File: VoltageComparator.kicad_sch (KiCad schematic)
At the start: 7 parts, among them U4 74LS08, U5 LM358

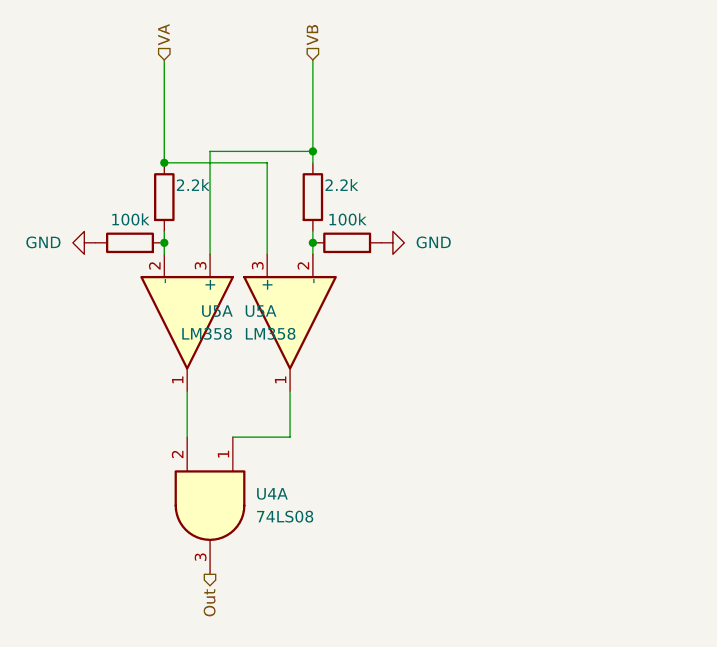
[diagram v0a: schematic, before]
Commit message: Added FSM, Button, 555 timer, changed shift registers
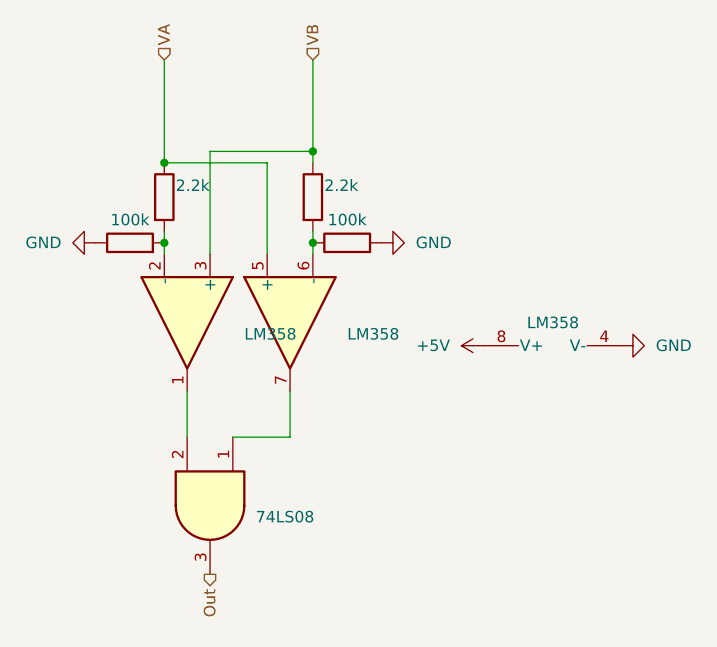
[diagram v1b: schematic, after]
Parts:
- added unit 2 of U18
- renumbered R9 to R5, R10 to R6, R11 to R7, R12 to R8, U5 to U18, U4 to U5
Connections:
- net GND: now also U18.4 (V-)
- net VA: now also U18.5 (+); no longer U18.3 (+)
- net at U5.1: now also U18.7; no longer U18.1
- net at R7.2, R8.1: now also U18.6 (-); no longer U18.2 (-)
- new net +5V: U18.8 (V+)
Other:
- title: (none) -> Voltage Tolerance Comparator

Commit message: Started PCB Work
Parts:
- removed unit 3 of U18
- R10: renamed from R7; value 2.2k -> 10k; footprint (none) -> Resistor_SMD:R_0805_2012Metric_Pad1.20x1.40mm_HandSolder
- R11: renamed from R8; value 100k -> 200k; footprint (none) -> Resistor_SMD:R_0805_2012Metric_Pad1.20x1.40mm_HandSolder
- R8: renamed from R5; value 100k -> 200k; footprint (none) -> Resistor_SMD:R_0805_2012Metric_Pad1.20x1.40mm_HandSolder
- R9: renamed from R6; footprint (none) -> Resistor_SMD:R_0805_2012Metric_Pad1.20x1.40mm_HandSolder
- U18: value LM358 -> LM324; footprint (none) -> Package_SO:SOIC-14_3.9x8.7mm_P1.27mm; symbol Amplifier_Operational:LM358 -> Amplifier_Operational:LM324
- U19: renamed from U5; footprint (none) -> Package_SO:SOIC-14_3.9x8.7mm_P1.27mm

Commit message: routed
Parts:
- renumbered R9 to R10, R10 to R11, R11 to R12, R8 to R9
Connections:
- net VA: now also U18.10 (+); no longer U18.5 (+)
- net VB: now also U18.12 (+); no longer U18.3 (+)
- net at U19.1: now also U18.8; no longer U18.7
- net at U19.2: now also U18.14; no longer U18.1
- net at R10.2, R9.2: now also U18.13 (-); no longer U18.2 (-)
- net at R11.2, R12.1: now also U18.9 (-); no longer U18.6 (-)
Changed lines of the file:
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@@
 		(on_board yes)
 		(dnp no)
-		(fields_autoplaced yes)
 		(property "Reference" "U19"
 			(at 58.42 95.2416 90)
@@
 		(dnp no)
 		(fields_autoplaced yes)
-		(property "Reference" "#PWR087"
+		(property "Reference" "#PWR088"
 			(at 78.74 67.31 0)
 			(effects
@@
 			(project "ECE145Mastermind"
 				(path "/8c64fe8a-5d6b-41bc-b3a3-9bda7b2e0f2c/218d925b-79f6-474b-97b2-c0ad78559cda"
-					(reference "#PWR091")
-					(unit 1)
-				)
-				(path "/8c64fe8a-5d6b-41bc-b3a3-9bda7b2e0f2c/4f59e726-7fd4-4ef0-8dbb-7a41976aa953"
-					(reference "#PWR087")
-					(unit 1)
-				)
-				(path "/8c64fe8a-5d6b-41bc-b3a3-9bda7b2e0f2c/acb554fe-df67-46ea-bc1c-079edbbfc216"
-					(reference "#PWR089")
-					(unit 1)
-				)
-				(path "/8c64fe8a-5d6b-41bc-b3a3-9bda7b2e0f2c/d4674d5d-47f2-4c8d-9fae-4e866cda3652"
-					(reference "#PWR093")
+					(reference "#PWR092")
+					(unit 1)
+				)
+				(path "/8c64fe8a-5d6b-41bc-b3a3-9bda7b2e0f2c/4f59e726-7fd4-4ef0-8dbb-7a41976aa953"
+					(reference "#PWR088")
+					(unit 1)
+				)
+				(path "/8c64fe8a-5d6b-41bc-b3a3-9bda7b2e0f2c/acb554fe-df67-46ea-bc1c-079edbbfc216"
+					(reference "#PWR090")
+					(unit 1)
+				)
+				(path "/8c64fe8a-5d6b-41bc-b3a3-9bda7b2e0f2c/d4674d5d-47f2-4c8d-9fae-4e866cda3652"
+					(reference "#PWR094")
 					(unit 1)
 				)
@@
 		(on_board yes)
 		(dnp no)
-		(property "Reference" "R9"
+		(property "Reference" "R10"
 			(at 50.8 60.9599 0)
 			(effects
@@
 			(project "ECE145Mastermind"
 				(path "/8c64fe8a-5d6b-41bc-b3a3-9bda7b2e0f2c/218d925b-79f6-474b-97b2-c0ad78559cda"
-					(reference "R17")
-					(unit 1)
-				)
-				(path "/8c64fe8a-5d6b-41bc-b3a3-9bda7b2e0f2c/4f59e726-7fd4-4ef0-8dbb-7a41976aa953"
-					(reference "R9")
-					(unit 1)
-				)
-				(path "/8c64fe8a-5d6b-41bc-b3a3-9bda7b2e0f2c/acb554fe-df67-46ea-bc1c-079edbbfc216"
-					(reference "R13")
-					(unit 1)
-				)
-				(path "/8c64fe8a-5d6b-41bc-b3a3-9bda7b2e0f2c/d4674d5d-47f2-4c8d-9fae-4e866cda3652"
-					(reference "R21")
+					(reference "R18")
+					(unit 1)
+				)
+				(path "/8c64fe8a-5d6b-41bc-b3a3-9bda7b2e0f2c/4f59e726-7fd4-4ef0-8dbb-7a41976aa953"
+					(reference "R10")
+					(unit 1)
+				)
+				(path "/8c64fe8a-5d6b-41bc-b3a3-9bda7b2e0f2c/acb554fe-df67-46ea-bc1c-079edbbfc216"
+					(reference "R14")
+					(unit 1)
+				)
+				(path "/8c64fe8a-5d6b-41bc-b3a3-9bda7b2e0f2c/d4674d5d-47f2-4c8d-9fae-4e866cda3652"
+					(reference "R22")
 					(unit 1)
 				)
@@
 		(dnp no)
 		(fields_autoplaced yes)
-		(property "Reference" "#PWR086"
+		(property "Reference" "#PWR087"
 			(at 34.29 67.31 0)
 			(effects
@@
 			(project "ECE145Mastermind"
 				(path "/8c64fe8a-5d6b-41bc-b3a3-9bda7b2e0f2c/218d925b-79f6-474b-97b2-c0ad78559cda"
-					(reference "#PWR090")
-					(unit 1)
-				)
-				(path "/8c64fe8a-5d6b-41bc-b3a3-9bda7b2e0f2c/4f59e726-7fd4-4ef0-8dbb-7a41976aa953"
-					(reference "#PWR086")
-					(unit 1)
-				)
-				(path "/8c64fe8a-5d6b-41bc-b3a3-9bda7b2e0f2c/acb554fe-df67-46ea-bc1c-079edbbfc216"
-					(reference "#PWR088")
-					(unit 1)
-				)
-				(path "/8c64fe8a-5d6b-41bc-b3a3-9bda7b2e0f2c/d4674d5d-47f2-4c8d-9fae-4e866cda3652"
-					(reference "#PWR092")
+					(reference "#PWR091")
+					(unit 1)
+				)
+				(path "/8c64fe8a-5d6b-41bc-b3a3-9bda7b2e0f2c/4f59e726-7fd4-4ef0-8dbb-7a41976aa953"
+					(reference "#PWR087")
+					(unit 1)
+				)
+				(path "/8c64fe8a-5d6b-41bc-b3a3-9bda7b2e0f2c/acb554fe-df67-46ea-bc1c-079edbbfc216"
+					(reference "#PWR089")
+					(unit 1)
+				)
+				(path "/8c64fe8a-5d6b-41bc-b3a3-9bda7b2e0f2c/d4674d5d-47f2-4c8d-9fae-4e866cda3652"
+					(reference "#PWR093")
 					(unit 1)
 				)
@@
 		(on_board yes)
 		(dnp no)
-		(property "Reference" "R10"
+		(property "Reference" "R11"
 			(at 67.31 60.9599 0)
 			(effects
@@
 			(project "ECE145Mastermind"
 				(path "/8c64fe8a-5d6b-41bc-b3a3-9bda7b2e0f2c/218d925b-79f6-474b-97b2-c0ad78559cda"
-					(reference "R18")
-					(unit 1)
-				)
-				(path "/8c64fe8a-5d6b-41bc-b3a3-9bda7b2e0f2c/4f59e726-7fd4-4ef0-8dbb-7a41976aa953"
-					(reference "R10")
-					(unit 1)
-				)
-				(path "/8c64fe8a-5d6b-41bc-b3a3-9bda7b2e0f2c/acb554fe-df67-46ea-bc1c-079edbbfc216"
-					(reference "R14")
-					(unit 1)
-				)
-				(path "/8c64fe8a-5d6b-41bc-b3a3-9bda7b2e0f2c/d4674d5d-47f2-4c8d-9fae-4e866cda3652"
-					(reference "R22")
+					(reference "R19")
+					(unit 1)
+				)
+				(path "/8c64fe8a-5d6b-41bc-b3a3-9bda7b2e0f2c/4f59e726-7fd4-4ef0-8dbb-7a41976aa953"
+					(reference "R11")
+					(unit 1)
+				)
+				(path "/8c64fe8a-5d6b-41bc-b3a3-9bda7b2e0f2c/acb554fe-df67-46ea-bc1c-079edbbfc216"
+					(reference "R15")
+					(unit 1)
+				)
+				(path "/8c64fe8a-5d6b-41bc-b3a3-9bda7b2e0f2c/d4674d5d-47f2-4c8d-9fae-4e866cda3652"
+					(reference "R23")
 					(unit 1)
 				)
@@
 		(at 62.23 76.2 90)
 		(mirror x)
-		(unit 2)
+		(unit 3)
 		(exclude_from_sim no)
 		(in_bom yes)
@@
 		)
 		(property "Value" "LM324"
-			(at 68.58 76.1999 90)
+			(at 68.58 77.4699 90)
 			(effects
 				(font
@@
 				(path "/8c64fe8a-5d6b-41bc-b3a3-9bda7b2e0f2c/4f59e726-7fd4-4ef0-8dbb-7a41976aa953"
 					(reference "U18")
+					(unit 3)
+				)
+				(path "/8c64fe8a-5d6b-41bc-b3a3-9bda7b2e0f2c/acb554fe-df67-46ea-bc1c-079edbbfc216"
+					(reference "U18")
 					(unit 2)
-				)
-				(path "/8c64fe8a-5d6b-41bc-b3a3-9bda7b2e0f2c/acb554fe-df67-46ea-bc1c-079edbbfc216"
-					(reference "U18")
-					(unit 4)
 				)
 				(path "/8c64fe8a-5d6b-41bc-b3a3-9bda7b2e0f2c/d4674d5d-47f2-4c8d-9fae-4e866cda3652"
@@
 		(lib_id "Amplifier_Operational:LM324")
 		(at 50.8 76.2 270)
-		(unit 1)
+		(unit 4)
 		(exclude_from_sim no)
 		(in_bom yes)
@@
 		)
 		(property "Value" "LM324"
-			(at 57.15 76.1999 90)
+			(at 57.15 77.4699 90)
 			(effects
 				(font
@@
 				(path "/8c64fe8a-5d6b-41bc-b3a3-9bda7b2e0f2c/4f59e726-7fd4-4ef0-8dbb-7a41976aa953"
 					(reference "U18")
-					(unit 1)
+					(unit 4)
 				)
 				(path "/8c64fe8a-5d6b-41bc-b3a3-9bda7b2e0f2c/acb554fe-df67-46ea-bc1c-079edbbfc216"
 					(reference "U18")
-					(unit 3)
+					(unit 1)
 				)
 				(path "/8c64fe8a-5d6b-41bc-b3a3-9bda7b2e0f2c/d4674d5d-47f2-4c8d-9fae-4e866cda3652"
@@
 		(on_board yes)
 		(dnp no)
-		(property "Reference" "R8"
+		(property "Reference" "R9"
 			(at 44.45 60.96 90)
 			(effects
@@
 			(project "ECE145Mastermind"
 				(path "/8c64fe8a-5d6b-41bc-b3a3-9bda7b2e0f2c/218d925b-79f6-474b-97b2-c0ad78559cda"
-					(reference "R16")
-					(unit 1)
-				)
-				(path "/8c64fe8a-5d6b-41bc-b3a3-9bda7b2e0f2c/4f59e726-7fd4-4ef0-8dbb-7a41976aa953"
-					(reference "R8")
-					(unit 1)
-				)
-				(path "/8c64fe8a-5d6b-41bc-b3a3-9bda7b2e0f2c/acb554fe-df67-46ea-bc1c-079edbbfc216"
-					(reference "R12")
-					(unit 1)
-				)
-				(path "/8c64fe8a-5d6b-41bc-b3a3-9bda7b2e0f2c/d4674d5d-47f2-4c8d-9fae-4e866cda3652"
-					(reference "R20")
+					(reference "R17")
+					(unit 1)
+				)
+				(path "/8c64fe8a-5d6b-41bc-b3a3-9bda7b2e0f2c/4f59e726-7fd4-4ef0-8dbb-7a41976aa953"
+					(reference "R9")
+					(unit 1)
+				)
+				(path "/8c64fe8a-5d6b-41bc-b3a3-9bda7b2e0f2c/acb554fe-df67-46ea-bc1c-079edbbfc216"
+					(reference "R13")
+					(unit 1)
+				)
+				(path "/8c64fe8a-5d6b-41bc-b3a3-9bda7b2e0f2c/d4674d5d-47f2-4c8d-9fae-4e866cda3652"
+					(reference "R21")
 					(unit 1)
 				)
@@
 		(on_board yes)
 		(dnp no)
-		(property "Reference" "R11"
+		(property "Reference" "R12"
 			(at 68.58 60.96 90)
 			(effects
@@
 			(project "ECE145Mastermind"
 				(path "/8c64fe8a-5d6b-41bc-b3a3-9bda7b2e0f2c/218d925b-79f6-474b-97b2-c0ad78559cda"
-					(reference "R19")
-					(unit 1)
-				)
-				(path "/8c64fe8a-5d6b-41bc-b3a3-9bda7b2e0f2c/4f59e726-7fd4-4ef0-8dbb-7a41976aa953"
-					(reference "R11")
-					(unit 1)
-				)
-				(path "/8c64fe8a-5d6b-41bc-b3a3-9bda7b2e0f2c/acb554fe-df67-46ea-bc1c-079edbbfc216"
-					(reference "R15")
-					(unit 1)
-				)
-				(path "/8c64fe8a-5d6b-41bc-b3a3-9bda7b2e0f2c/d4674d5d-47f2-4c8d-9fae-4e866cda3652"
-					(reference "R23")
-					(unit 1)
-				)
+					(reference "R20")
+					(unit 1)
+				)
+				(path "/8c64fe8a-5d6b-41bc-b3a3-9bda7b2e0f2c/4f59e726-7fd4-4ef0-8dbb-7a41976aa953"
+					(reference "R12")
+					(unit 1)
+				)
+				(path "/8c64fe8a-5d6b-41bc-b3a3-9bda7b2e0f2c/acb554fe-df67-46ea-bc1c-079edbbfc216"
+					(reference "R16")
+					(unit 1)
+				)
+				(path "/8c64fe8a-5d6b-41bc-b3a3-9bda7b2e0f2c/d4674d5d-47f2-4c8d-9fae-4e866cda3652"
+					(reference "R24")
+					(unit 1)
+				)
